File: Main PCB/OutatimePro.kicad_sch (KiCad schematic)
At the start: 47 parts, among them IC1 PAM8904JPR, J1 USB_B_Micro_PCB_Edge_receptac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, J2 FH35C-9S-0.3SHW, J3 OSO_SWD, Q1 ALS-PT19-315C/L177/TR8, SW1 EVPAWED40, U1 ATSAML22N18A-CFUT, U2 MIC5365-3.3YMT, U3 USBLC6-2P6, U4 MAX40200ANS, Y1 32.768kHz

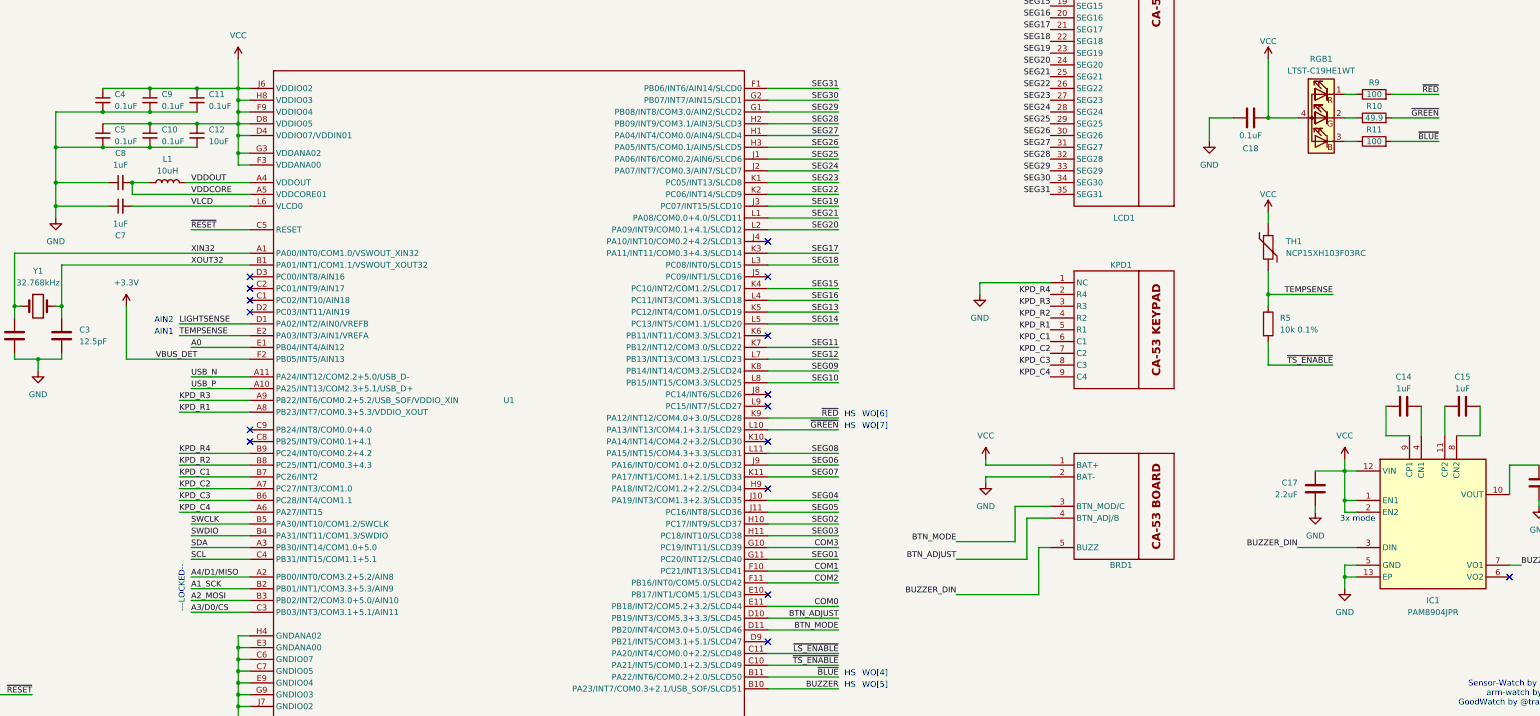
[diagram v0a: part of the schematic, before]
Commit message: Change keypad/button pins for available interrupts
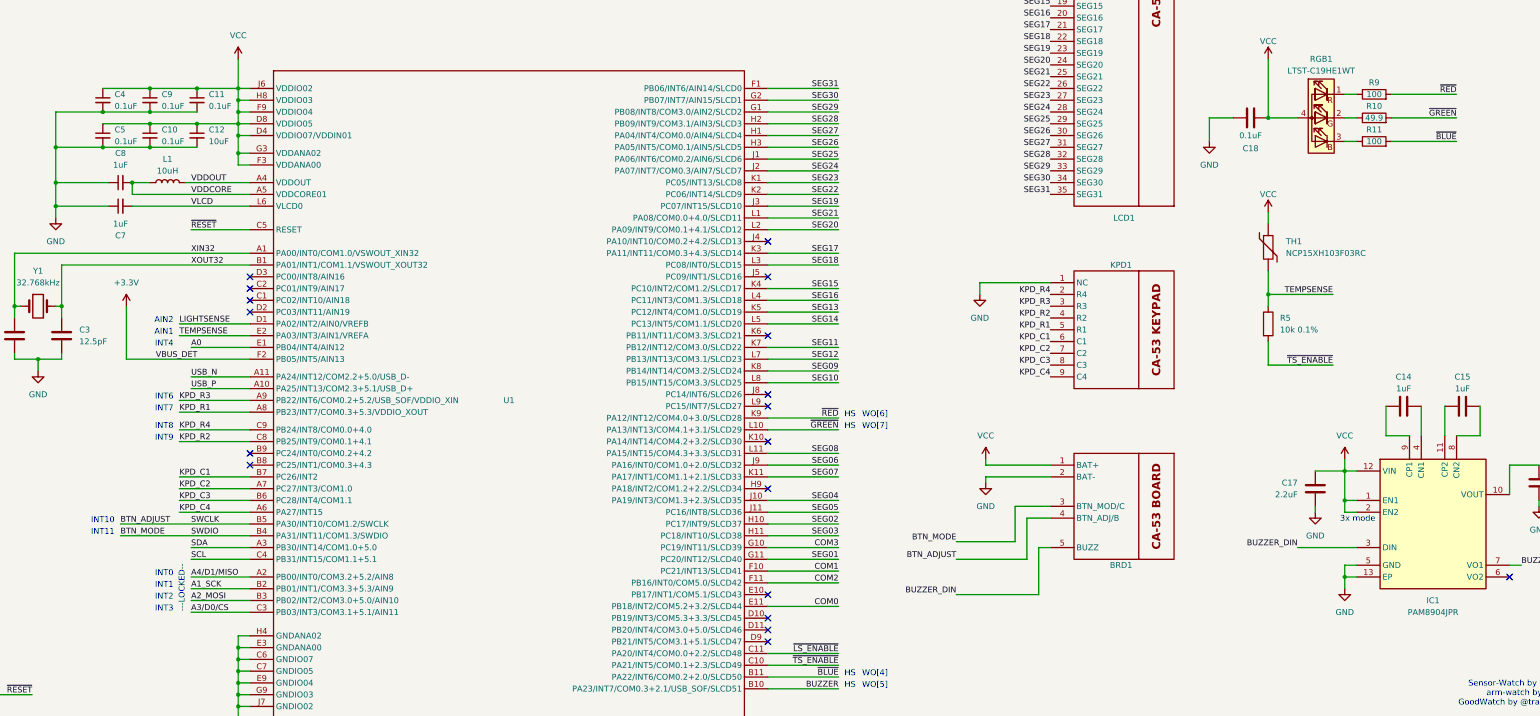
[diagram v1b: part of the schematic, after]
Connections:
- net SWCLK is gone; now on net BTN_ADJUST: J3.4 (SWCLK), U1.B5 (PA30/INT10/COM1.2/SWCLK)
- net SWDIO is gone; now on net BTN_MODE: J3.1 (SWDIO), U1.B4 (PA31/INT11/COM1.3/SWDIO)
- net BTN_ADJUST: no longer U1.D10 (PB19/INT3/COM5.3+3.3/SLCD45)
- net BTN_MODE: no longer U1.D11 (PB20/INT4/COM3.0+5.0/SLCD46)
- net KPD_R2: now also U1.C8 (PB25/INT9/COM0.1+4.1); no longer U1.B8 (PC25/INT1/COM0.3+4.3)
- net KPD_R4: now also U1.C9 (PB24/INT8/COM0.0+4.0); no longer U1.B9 (PC24/INT0/COM0.2+4.2)
- no-connect marks 17 -> 19
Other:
- note added: "INT0"
- note added: "INT1"
- note added: "INT10"
- note added: "INT11"
- note added: "INT2"
- note added: "INT3"
- note added: "INT4"
- note added: "INT6"
- note added: "INT7"
- note added: "INT8"
- note added: "INT9"

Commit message: rename seg/com numbers to reflect firmware, fix up batt/vcc change circuitry
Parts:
- removed R8: 10k, Resistor_SMD:R_0402_1005Metric, symbol Device:R
- added U5: MAX40200ANS, Package_BGA:WLP-4_0.728x0.728mm_Layout2x2_P0.35mm, symbol Analog_Switch:MAX40200ANS
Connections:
- net COM3 is gone; now on net COM2: LCD1.4 (COM3), U1.G10 (PC19/INT11/SLCD39)
- net KPD_C4 is gone; now on net KPD_C3: KPD1.9 (C4), U1.A6 (PA27/INT15)
- net KPD_R4 is gone; now on net KPD_R3: KPD1.2 (R4), U1.C9 (PB24/INT8/COM0.0+4.0)
- net SEG31 is gone; now on net SEG30: LCD1.35 (SEG31), U1.F1 (PB06/INT6/AIN14/SLCD0)
- net COM0: now also LCD1.2 (COM1), U1.F10 (PC21/INT13/SLCD41); no longer LCD1.1 (COM0), U1.E11 (PB18/INT2/COM5.2+3.2/SLCD44)
- net COM1: now also LCD1.3 (COM2), U1.F11 (PB16/INT0/COM5.0/SLCD42); no longer LCD1.2 (COM1), U1.F10 (PC21/INT13/SLCD41)
- net COM2: no longer LCD1.3 (COM2), U1.F11 (PB16/INT0/COM5.0/SLCD42)
- net GND: now also U5.B2 (GND)
- net KPD_C1: now also KPD1.7 (C2), U1.A7 (PC27/INT3/COM1.0); no longer KPD1.6 (C1), U1.B7 (PC26/INT2)
- net KPD_C2: now also KPD1.8 (C3), U1.B6 (PC28/INT4/COM1.1); no longer KPD1.7 (C2), U1.A7 (PC27/INT3/COM1.0)
- net KPD_C3: no longer KPD1.8 (C3), U1.B6 (PC28/INT4/COM1.1)
- net KPD_R1: now also KPD1.4 (R2), U1.C8 (PB25/INT9/COM0.1+4.1); no longer KPD1.5 (R1), U1.A8 (PB23/INT7/COM0.3+5.3/VDDIO_XOUT)
- net KPD_R2: now also KPD1.3 (R3), U1.A9 (PB22/INT6/COM0.2+5.2/USB_SOF/VDDIO_XIN); no longer KPD1.4 (R2), U1.C8 (PB25/INT9/COM0.1+4.1)
- net KPD_R3: no longer KPD1.3 (R3), U1.A9 (PB22/INT6/COM0.2+5.2/USB_SOF/VDDIO_XIN)
- net SEG01: now also LCD1.6 (SEG02), U1.H10 (PC17/INT9/SLCD37); no longer LCD1.5 (SEG01), U1.G11 (PC20/INT12/SLCD40)
- net SEG02: now also LCD1.7 (SEG03), U1.H11 (PC18/INT10/SLCD38); no longer LCD1.6 (SEG02), U1.H10 (PC17/INT9/SLCD37)
- net SEG03: now also LCD1.8 (SEG04), U1.J10 (PA19/INT3/COM1.3+2.3/SLCD35); no longer LCD1.7 (SEG03), U1.H11 (PC18/INT10/SLCD38)
- net SEG04: now also LCD1.9 (SEG05), U1.J11 (PC16/INT8/SLCD36); no longer LCD1.8 (SEG04), U1.J10 (PA19/INT3/COM1.3+2.3/SLCD35)
- net SEG05: now also LCD1.10 (SEG06), U1.J9 (PA16/INT0/COM1.0+2.0/SLCD32); no longer LCD1.9 (SEG05), U1.J11 (PC16/INT8/SLCD36)
- net SEG06: now also LCD1.11 (SEG07), U1.K11 (PA17/INT1/COM1.1+2.1/SLCD33); no longer LCD1.10 (SEG06), U1.J9 (PA16/INT0/COM1.0+2.0/SLCD32)
- net SEG07: now also LCD1.12 (SEG08), U1.L11 (PA15/INT15/COM4.3+3.3/SLCD31); no longer LCD1.11 (SEG07), U1.K11 (PA17/INT1/COM1.1+2.1/SLCD33)
- net SEG08: now also LCD1.13 (SEG09), U1.K8 (PB14/INT14/COM3.2/SLCD24); no longer LCD1.12 (SEG08), U1.L11 (PA15/INT15/COM4.3+3.3/SLCD31)
- net SEG09: now also LCD1.14 (SEG10), U1.L8 (PB15/INT15/COM3.3/SLCD25); no longer LCD1.13 (SEG09), U1.K8 (PB14/INT14/COM3.2/SLCD24)
- net SEG10: now also LCD1.15 (SEG11), U1.K7 (PB12/INT12/COM3.0/SLCD22); no longer LCD1.14 (SEG10), U1.L8 (PB15/INT15/COM3.3/SLCD25)
- net SEG11: now also LCD1.16 (SEG12), U1.L7 (PB13/INT13/COM3.1/SLCD23); no longer LCD1.15 (SEG11), U1.K7 (PB12/INT12/COM3.0/SLCD22)
- net SEG12: now also LCD1.17 (SEG13), U1.K5 (PC12/INT4/COM1.0/SLCD19); no longer LCD1.16 (SEG12), U1.L7 (PB13/INT13/COM3.1/SLCD23)
- net SEG13: now also LCD1.18 (SEG14), U1.L5 (PC13/INT5/COM1.1/SLCD20); no longer LCD1.17 (SEG13), U1.K5 (PC12/INT4/COM1.0/SLCD19)
- net SEG14: now also LCD1.19 (SEG15), U1.K4 (PC10/INT2/COM1.2/SLCD17); no longer LCD1.18 (SEG14), U1.L5 (PC13/INT5/COM1.1/SLCD20)
- net SEG15: now also LCD1.20 (SEG16), U1.L4 (PC11/INT3/COM1.3/SLCD18); no longer LCD1.19 (SEG15), U1.K4 (PC10/INT2/COM1.2/SLCD17)
- net SEG16: now also LCD1.21 (SEG17), U1.K3 (PA11/INT11/COM0.3+4.3/SLCD14); no longer LCD1.20 (SEG16), U1.L4 (PC11/INT3/COM1.3/SLCD18)
- net SEG17: now also LCD1.22 (SEG18), U1.L3 (PC08/INT0/SLCD15); no longer LCD1.21 (SEG17), U1.K3 (PA11/INT11/COM0.3+4.3/SLCD14)
- net SEG18: now also LCD1.23 (SEG19), U1.J3 (PC07/INT15/SLCD10); no longer LCD1.22 (SEG18), U1.L3 (PC08/INT0/SLCD15)
- net SEG19: now also LCD1.24 (SEG20), U1.L2 (PA09/INT9/COM0.1+4.1/SLCD12); no longer LCD1.23 (SEG19), U1.J3 (PC07/INT15/SLCD10)
- net SEG20: now also LCD1.25 (SEG21), U1.L1 (PA08/COM0.0+4.0/SLCD11); no longer LCD1.24 (SEG20), U1.L2 (PA09/INT9/COM0.1+4.1/SLCD12)
- net SEG21: now also LCD1.26 (SEG22), U1.K2 (PC06/INT14/SLCD9); no longer LCD1.25 (SEG21), U1.L1 (PA08/COM0.0+4.0/SLCD11)
- net SEG22: now also LCD1.27 (SEG23), U1.K1 (PC05/INT13/SLCD8); no longer LCD1.26 (SEG22), U1.K2 (PC06/INT14/SLCD9)
- net SEG23: now also LCD1.28 (SEG24), U1.J2 (PA07/INT7/COM0.3/AIN7/SLCD7); no longer LCD1.27 (SEG23), U1.K1 (PC05/INT13/SLCD8)
- net SEG24: now also LCD1.29 (SEG25), U1.J1 (PA06/INT6/COM0.2/AIN6/SLCD6); no longer LCD1.28 (SEG24), U1.J2 (PA07/INT7/COM0.3/AIN7/SLCD7)
- net SEG25: now also LCD1.30 (SEG26), U1.H3 (PA05/INT5/COM0.1/AIN5/SLCD5); no longer LCD1.29 (SEG25), U1.J1 (PA06/INT6/COM0.2/AIN6/SLCD6)
- net SEG26: now also LCD1.31 (SEG27), U1.H1 (PA04/INT4/COM0.0/AIN4/SLCD4); no longer LCD1.30 (SEG26), U1.H3 (PA05/INT5/COM0.1/AIN5/SLCD5)
- net SEG27: now also LCD1.32 (SEG28), U1.H2 (PB09/INT9/COM3.1/AIN3/SLCD3); no longer LCD1.31 (SEG27), U1.H1 (PA04/INT4/COM0.0/AIN4/SLCD4)
- net SEG28: now also LCD1.33 (SEG29), U1.G1 (PB08/INT8/COM3.0/AIN2/SLCD2); no longer LCD1.32 (SEG28), U1.H2 (PB09/INT9/COM3.1/AIN3/SLCD3)
- net SEG29: now also U1.G2 (PB07/INT7/AIN15/SLCD1); no longer LCD1.33 (SEG29), U1.G1 (PB08/INT8/COM3.0/AIN2/SLCD2)
- net SEG30: no longer LCD1.34 (SEG30), U1.G2 (PB07/INT7/AIN15/SLCD1)
- net VCC: now also U5.A2 (OUT); no longer BRD1.1 (BAT+)
- new net +BATT: BRD1.1 (BAT+), U5.A1 (VDD), U5.B1 (EN)
- new net KPD_C0: KPD1.6 (C1), U1.B7 (PC26/INT2)
- new net KPD_R0: KPD1.5 (R1), U1.A8 (PB23/INT7/COM0.3+5.3/VDDIO_XOUT)
- new net LCD_NC: LCD1.1 (COM0), U1.E11 (PB18/INT2/COM5.2+3.2/SLCD44)
- new net SEG00: LCD1.5 (SEG01), U1.G11 (PC20/INT12/SLCD40)
- new net SEG39: LCD1.34 (SEG30)
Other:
- note added: "AIN0"
- note added: "No signal measured"
- note removed: "AIN2"
- moved on the sheet: BRD1, C1, C10, C11, C12, C14, C15, C16, C17, C18, C2, C3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

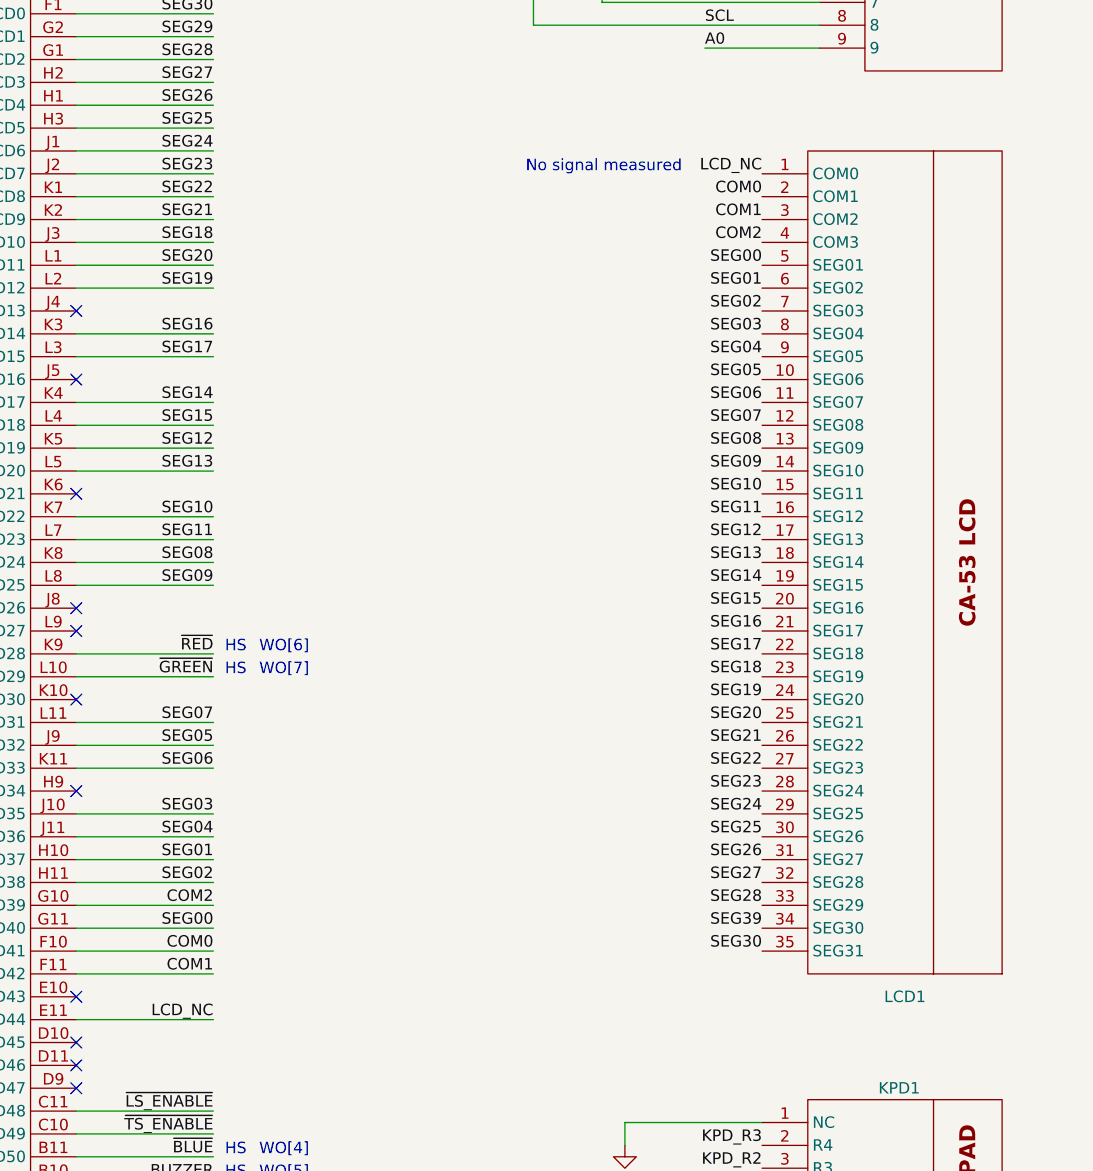
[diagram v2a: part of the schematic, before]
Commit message: remove lcd mapping pcb and add lcsc component numbers to fpc board
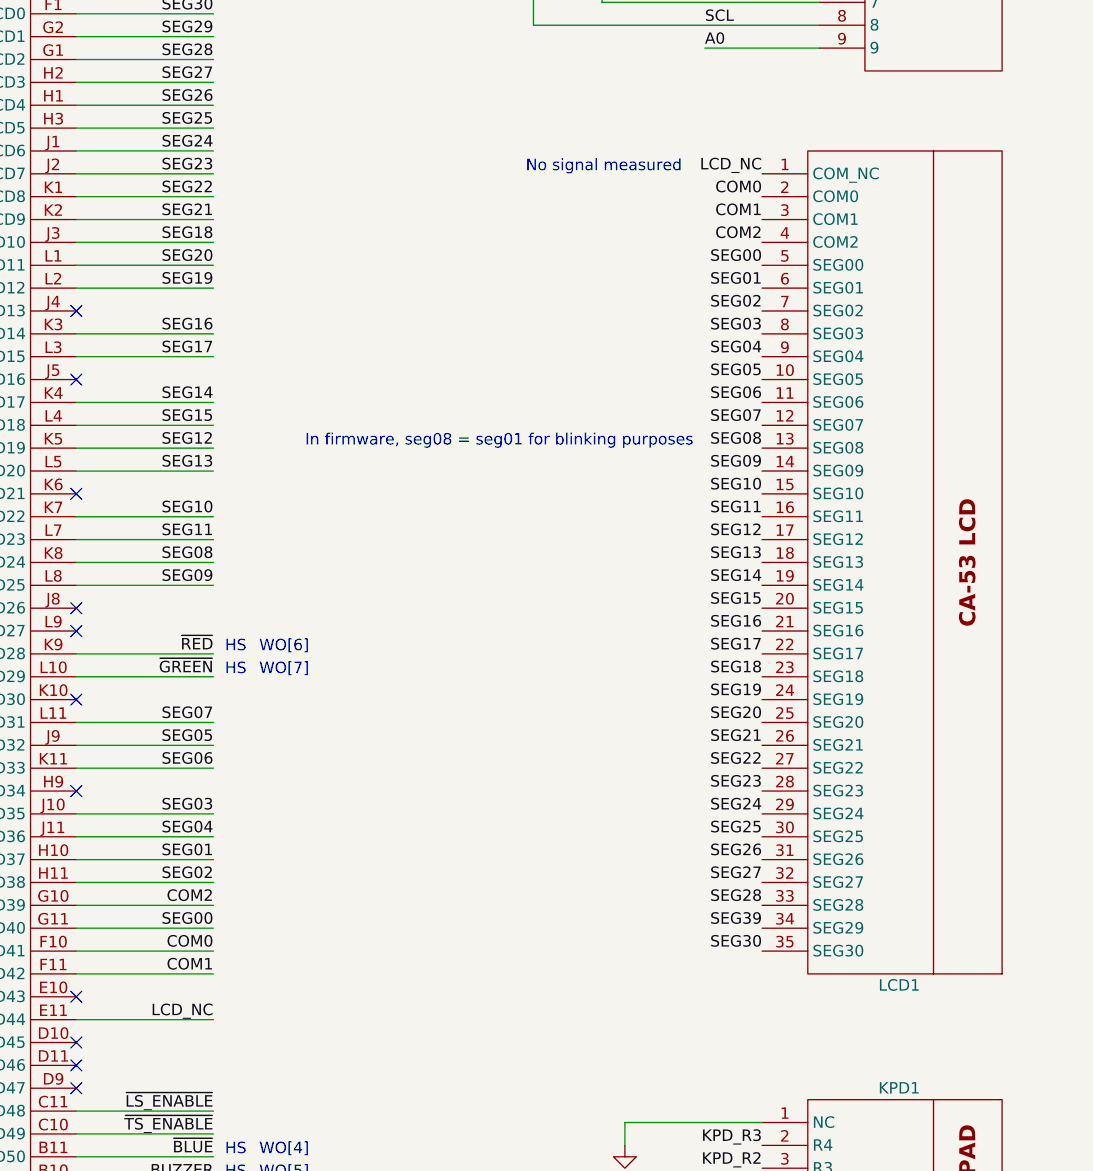
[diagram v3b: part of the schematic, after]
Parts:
- J3, TP1, TP2, TP3, TP4: now left out of the parts list
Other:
- note added: "In firmware, seg08 = seg01 for blinking purposes"
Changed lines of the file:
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@@
 		)
 	)
+	(text "In firmware, seg08 = seg01 for blinking purposes"
+		(exclude_from_sim no)
+		(at 425.45 107.95 0)
+		(effects
+			(font
+				(size 1.27 1.27)
+			)
+			(justify right bottom)
+		)
+	)
 	(junction
 		(at 467.36 45.72)
@@
 		(body_style 1)
 		(exclude_from_sim no)
-		(in_bom yes)
+		(in_bom no)
 		(on_board yes)
-		(in_pos_files yes)
+		(in_pos_files no)
 		(dnp no)
 		(fields_autoplaced yes)
@@
 		(body_style 1)
 		(exclude_from_sim no)
-		(in_bom yes)
+		(in_bom no)
 		(on_board yes)
-		(in_pos_files yes)
+		(in_pos_files no)
 		(dnp no)
 		(fields_autoplaced yes)
@@
 		(body_style 1)
 		(exclude_from_sim no)
-		(in_bom yes)
+		(in_bom no)
 		(on_board yes)
-		(in_pos_files yes)
+		(in_pos_files no)
 		(dnp no)
 		(property "Reference" "TP2"
@@
 		(in_bom no)
 		(on_board yes)
-		(in_pos_files yes)
+		(in_pos_files no)
 		(dnp no)
 		(property "Reference" "KPD1"
@@
 		(dnp no)
 		(property "Reference" "LCD1"
-			(at 448.945 168.91 0)
+			(at 448.31 167.64 0)
 			(show_name no)
 			(do_not_autoplace no)
@@
 			)
 		)
-		(property "LCSC Part #" ""
-			(at 438.15 120.65 0)
-			(hide yes)
-			(show_name no)
-			(do_not_autoplace no)
-			(effects
-				(font
-					(size 1.27 1.27)
-				)
-			)
-		)
-		(property "Max Height" ""
-			(at 438.15 120.65 0)
-			(hide yes)
-			(show_name no)
-			(do_not_autoplace no)
-			(effects
-				(font
-					(size 1.27 1.27)
-				)
-			)
-		)
 		(pin "13"
 		)
@@
 		(body_style 1)
 		(exclude_from_sim no)
-		(in_bom yes)
+		(in_bom no)
 		(on_board yes)
-		(in_pos_files yes)
+		(in_pos_files no)
 		(dnp no)
 		(property "Reference" "TP4"
@@
 		(body_style 1)
 		(exclude_from_sim no)
-		(in_bom yes)
+		(in_bom no)
 		(on_board yes)
-		(in_pos_files yes)
+		(in_pos_files no)
 		(dnp no)
 		(fields_autoplaced yes)

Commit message: Remove FPC connector, put IMU on main pcb
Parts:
- removed J2: FH35C-9S-0.3SHW, OutatimePro:FH35-9S-0.3SHW, symbol OutatimePro:FH35-9S-0.3SHW
- added C19, C21: 0.1uF, Capacitor_SMD:C_0402_1005Metric, symbol Device:C_Small
- added C20: 10uF, Capacitor_SMD:C_0603_1608Metric, symbol Device:C_Small
- added U6: LIS2DW12TR, OutatimePro:LGA-12_2x2mm_P0.5mm, symbol Sensor_Motion:LIS2DE12
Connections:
- net A3/D0/CS: now also U6.11 (INT2)
- net A4/D1/MISO: now also U6.12 (INT1)
- net GND: now also C19.2, C20.2, C21.2, U6.5 (RES), U6.6 (GND), U6.7 (GND), U6.8 (GND)
- net SCL: now also U6.1 (SCL/SPC)
- net SDA: now also U6.4 (SDA/SDI)
- net VCC: now also C19.1, C20.1, C21.1, U6.10 (Vdd_IO), U6.2 (~{CS}), U6.3 (SA0/SDO), U6.9 (Vdd)
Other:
- moved on the sheet: R6, R7
